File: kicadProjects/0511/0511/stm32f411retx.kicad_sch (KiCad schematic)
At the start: 22 parts, among them SW68 SW_Push, U6 STM32F411RETx, Y1 32.768KHz, Y2 8MHz

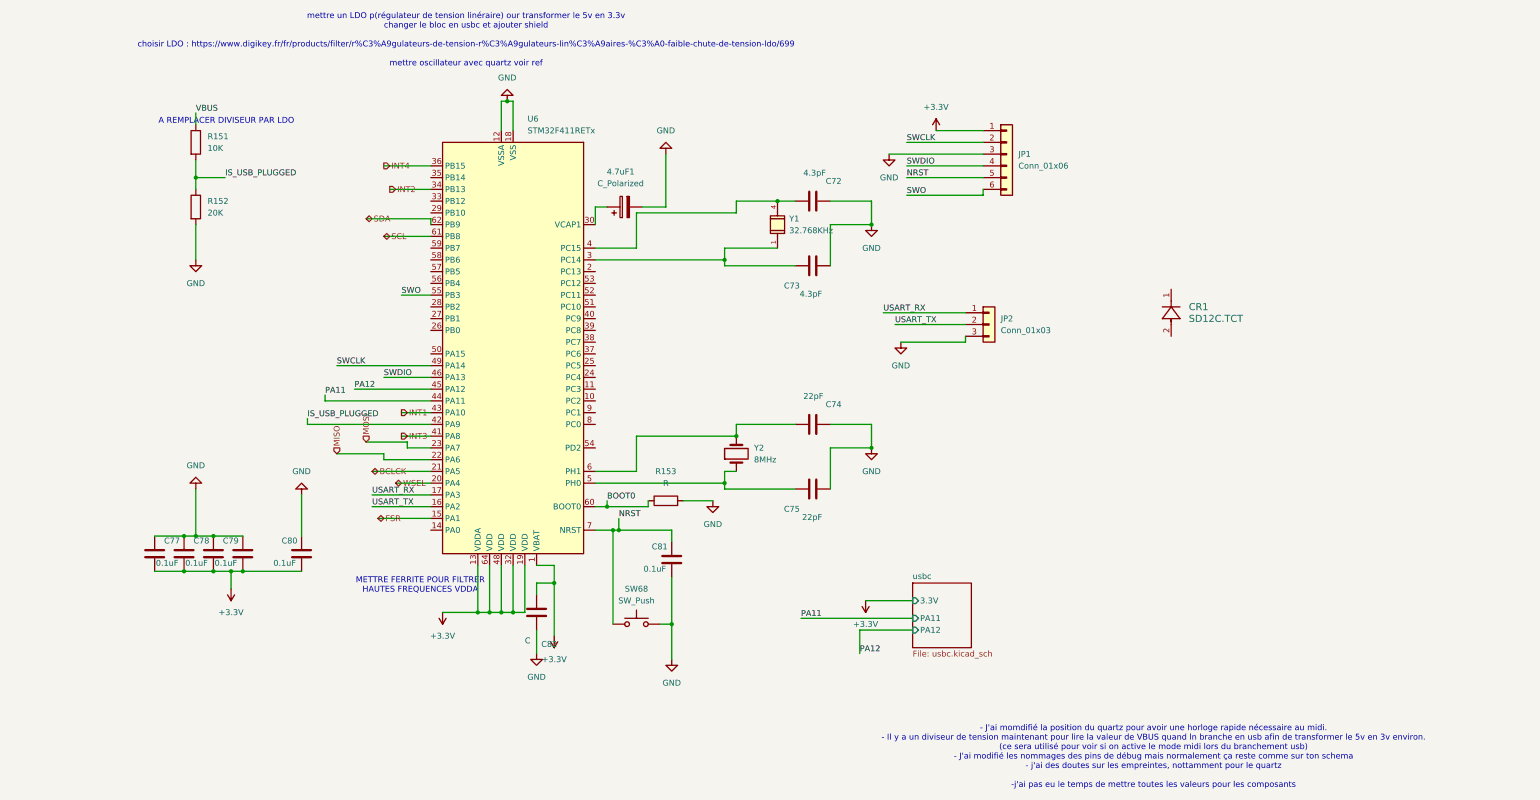
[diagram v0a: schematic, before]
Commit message: started to annotate and place buttons on pcb
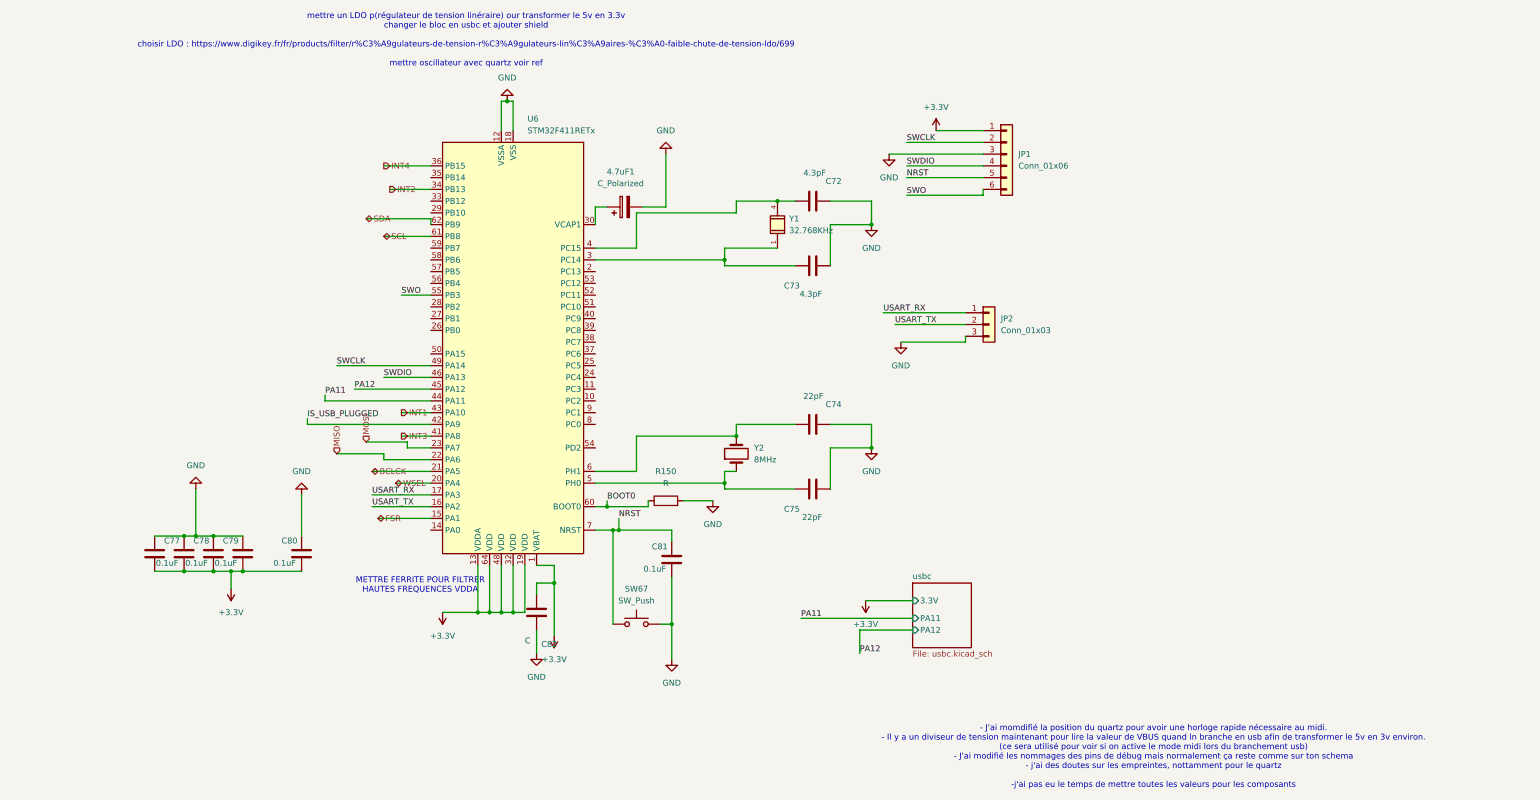
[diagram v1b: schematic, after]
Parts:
- removed CR1: SD12C.TCT, Project:CR_SD05_SEM, symbol ABS25-32.768KHZ-6-T:SD12C.TCT
- removed R151: 10K, Resistor_SMD:R_0603_1608Metric, symbol Device:R
- removed R152: 20K, Resistor_SMD:R_0603_1608Metric, symbol Device:R
- renumbered R153 to R150, SW68 to SW67
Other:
- note removed: "A REMPLACER DIVISEUR PAR LDO"

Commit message: poursuite placement et nommage références
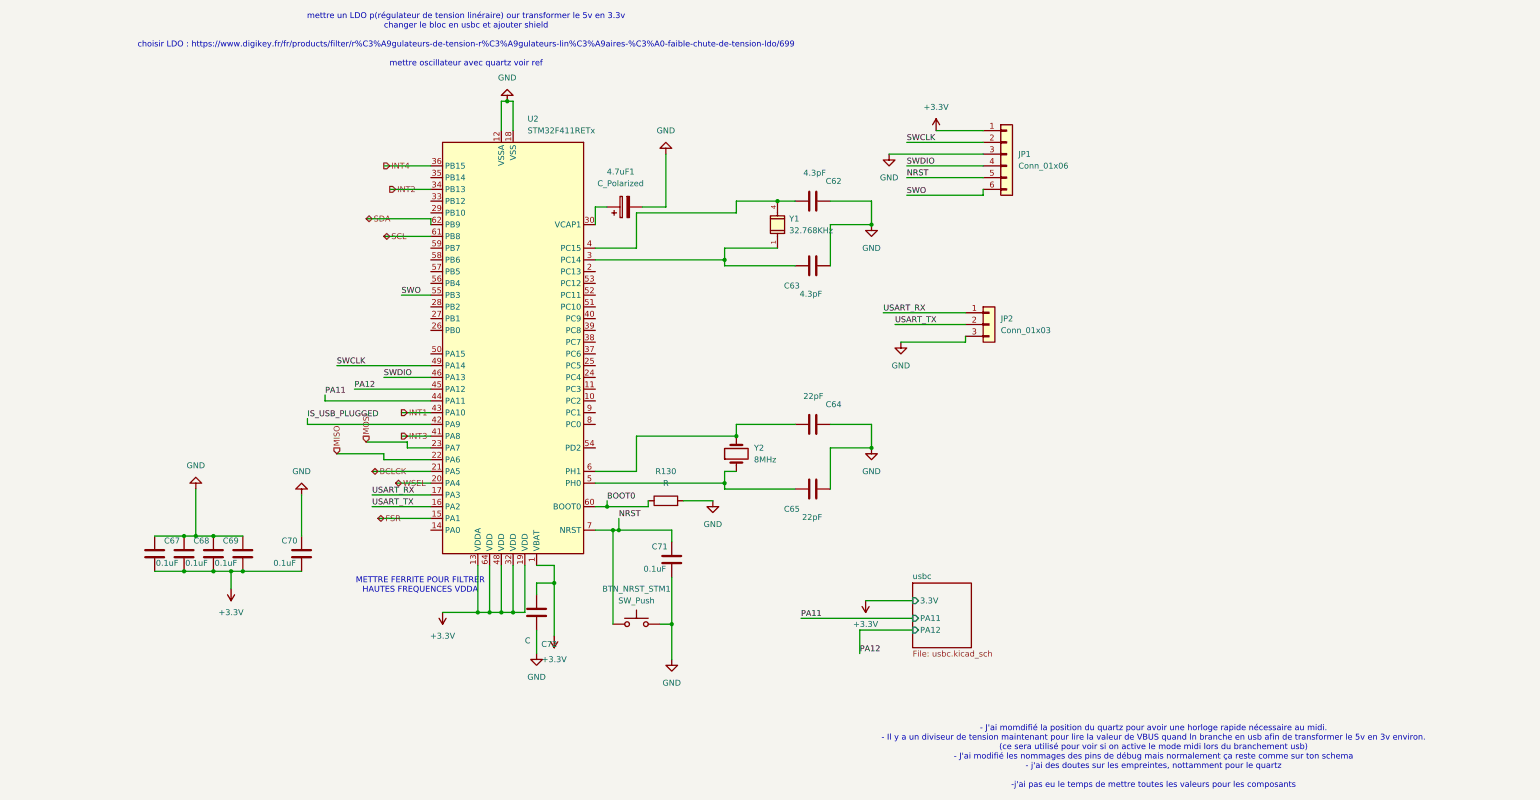
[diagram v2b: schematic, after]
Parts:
- renumbered SW67 to BTN_NRST_STM1, C72 to C62, C73 to C63, C74 to C64, C75 to C65, C76 to C66, C77 to C67, C78 to C68, C79 to C69, C80 to C70, C81 to C71, C82 to C72, R150 to R130, U6 to U2
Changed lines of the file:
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@@
 		(on_board yes)
 		(dnp no)
-		(property "Reference" "C77"
+		(property "Reference" "C67"
 			(at 23.622 129.286 0)
 			(effects
@@
 			(project "0511"
 				(path "/2c0b0e0d-c5e7-48b7-93bb-9be1941509af/7f025c79-ea20-4013-a71e-871359ae3c80"
-					(reference "C77")
+					(reference "C67")
 					(unit 1)
 				)
@@
 		(on_board yes)
 		(dnp no)
-		(property "Reference" "C74"
+		(property "Reference" "C64"
 			(at 166.624 99.822 90)
 			(effects
@@
 			(project "0511"
 				(path "/2c0b0e0d-c5e7-48b7-93bb-9be1941509af/7f025c79-ea20-4013-a71e-871359ae3c80"
-					(reference "C74")
+					(reference "C64")
 					(unit 1)
 				)
@@
 		(on_board yes)
 		(dnp no)
-		(property "Reference" "C80"
+		(property "Reference" "C70"
 			(at 49.022 129.286 0)
 			(effects
@@
 			(project "0511"
 				(path "/2c0b0e0d-c5e7-48b7-93bb-9be1941509af/7f025c79-ea20-4013-a71e-871359ae3c80"
-					(reference "C80")
+					(reference "C70")
 					(unit 1)
 				)
@@
 		(dnp no)
 		(fields_autoplaced yes)
-		(property "Reference" "#PWR0183"
+		(property "Reference" "#PWR0177"
 			(at 30.48 111.76 0)
 			(effects
@@
 			(project "0511"
 				(path "/2c0b0e0d-c5e7-48b7-93bb-9be1941509af/7f025c79-ea20-4013-a71e-871359ae3c80"
-					(reference "#PWR0183")
+					(reference "#PWR0177")
 					(unit 1)
 				)
@@
 		(dnp no)
 		(fields_autoplaced yes)
-		(property "Reference" "#PWR0184"
+		(property "Reference" "#PWR0178"
 			(at 53.34 113.03 0)
 			(effects
@@
 			(project "0511"
 				(path "/2c0b0e0d-c5e7-48b7-93bb-9be1941509af/7f025c79-ea20-4013-a71e-871359ae3c80"
-					(reference "#PWR0184")
+					(reference "#PWR0178")
 					(unit 1)
 				)
@@
 		(dnp no)
 		(fields_autoplaced yes)
-		(property "Reference" "U6"
+		(property "Reference" "U2"
 			(at 102.1781 38.1 0)
 			(effects
@@
 			(project "0511"
 				(path "/2c0b0e0d-c5e7-48b7-93bb-9be1941509af/7f025c79-ea20-4013-a71e-871359ae3c80"
-					(reference "U6")
+					(reference "U2")
 					(unit 1)
 				)
@@
 		(dnp no)
 		(fields_autoplaced yes)
-		(property "Reference" "R150"
+		(property "Reference" "R130"
 			(at 132.08 114.3 90)
 			(effects
@@
 			(project ""
 				(path "/2c0b0e0d-c5e7-48b7-93bb-9be1941509af/7f025c79-ea20-4013-a71e-871359ae3c80"
-					(reference "R150")
+					(reference "R130")
 					(unit 1)
 				)
@@
 		(dnp no)
 		(fields_autoplaced yes)
-		(property "Reference" "#PWR0178"
+		(property "Reference" "#PWR0172"
 			(at 132.08 39.37 0)
 			(effects
@@
 			(project "0511"
 				(path "/2c0b0e0d-c5e7-48b7-93bb-9be1941509af/7f025c79-ea20-4013-a71e-871359ae3c80"
-					(reference "#PWR0178")
+					(reference "#PWR0172")
 					(unit 1)
 				)
@@
 		(on_board yes)
 		(dnp no)
-		(property "Reference" "C73"
+		(property "Reference" "C63"
 			(at 161.036 74.168 90)
 			(effects
@@
 			(project "0511"
 				(path "/2c0b0e0d-c5e7-48b7-93bb-9be1941509af/7f025c79-ea20-4013-a71e-871359ae3c80"
-					(reference "C73")
+					(reference "C63")
 					(unit 1)
 				)
@@
 		(dnp no)
 		(fields_autoplaced yes)
-		(property "Reference" "#PWR0179"
+		(property "Reference" "#PWR0173"
 			(at 180.34 52.07 0)
 			(effects
@@
 			(project "0511"
 				(path "/2c0b0e0d-c5e7-48b7-93bb-9be1941509af/7f025c79-ea20-4013-a71e-871359ae3c80"
-					(reference "#PWR0179")
+					(reference "#PWR0173")
 					(unit 1)
 				)
@@
 		(dnp no)
 		(fields_autoplaced yes)
-		(property "Reference" "#PWR0185"
+		(property "Reference" "#PWR0179"
 			(at 142.24 127 0)
 			(effects
@@
 			(project "0511"
 				(path "/2c0b0e0d-c5e7-48b7-93bb-9be1941509af/7f025c79-ea20-4013-a71e-871359ae3c80"
-					(reference "#PWR0185")
+					(reference "#PWR0179")
 					(unit 1)
 				)
@@
 		(on_board yes)
 		(dnp no)
-		(property "Reference" "C72"
+		(property "Reference" "C62"
 			(at 166.624 51.562 90)
 			(effects
@@
 			(project "0511"
 				(path "/2c0b0e0d-c5e7-48b7-93bb-9be1941509af/7f025c79-ea20-4013-a71e-871359ae3c80"
-					(reference "C72")
+					(reference "C62")
 					(unit 1)
 				)
@@
 		(on_board yes)
 		(dnp no)
-		(property "Reference" "C78"
+		(property "Reference" "C68"
 			(at 29.972 129.286 0)
 			(effects
@@
 			(project "0511"
 				(path "/2c0b0e0d-c5e7-48b7-93bb-9be1941509af/7f025c79-ea20-4013-a71e-871359ae3c80"
-					(reference "C78")
+					(reference "C68")
 					(unit 1)
 				)
@@
 		(dnp no)
 		(fields_autoplaced yes)
-		(property "Reference" "#PWR0187"
+		(property "Reference" "#PWR0181"
 			(at 175.26 138.43 0)
 			(effects
@@
 			(project "0511"
 				(path "/2c0b0e0d-c5e7-48b7-93bb-9be1941509af/7f025c79-ea20-4013-a71e-871359ae3c80"
-					(reference "#PWR0187")
+					(reference "#PWR0181")
 					(unit 1)
 				)
@@
 		(dnp no)
 		(fields_autoplaced yes)
-		(property "Reference" "#PWR0181"
+		(property "Reference" "#PWR0175"
 			(at 182.88 92.71 0)
 			(effects
@@
 			(project "0511"
 				(path "/2c0b0e0d-c5e7-48b7-93bb-9be1941509af/7f025c79-ea20-4013-a71e-871359ae3c80"
-					(reference "#PWR0181")
+					(reference "#PWR0175")
 					(unit 1)
 				)
@@
 		(on_board yes)
 		(dnp no)
-		(property "Reference" "C76"
+		(property "Reference" "C66"
 			(at 17.272 129.286 0)
 			(effects
@@
 			(project "0511"
 				(path "/2c0b0e0d-c5e7-48b7-93bb-9be1941509af/7f025c79-ea20-4013-a71e-871359ae3c80"
-					(reference "C76")
+					(reference "C66")
 					(unit 1)
 				)
@@
 		(dnp no)
 		(fields_autoplaced yes)
-		(property "Reference" "#PWR0191"
+		(property "Reference" "#PWR0185"
 			(at 133.35 161.29 0)
 			(effects
@@
 			(project "0511"
 				(path "/2c0b0e0d-c5e7-48b7-93bb-9be1941509af/7f025c79-ea20-4013-a71e-871359ae3c80"
-					(reference "#PWR0191")
+					(reference "#PWR0185")
 					(unit 1)
 				)
@@
 		(dnp no)
 		(fields_autoplaced yes)
-		(property "Reference" "#PWR0190"
+		(property "Reference" "#PWR0184"
 			(at 104.14 160.02 0)
 			(effects
@@
 			(project "0511"
 				(path "/2c0b0e0d-c5e7-48b7-93bb-9be1941509af/7f025c79-ea20-4013-a71e-871359ae3c80"
-					(reference "#PWR0190")
+					(reference "#PWR0184")
 					(unit 1)
 				)
@@
 		(on_board yes)
 		(dnp no)
-		(property "Reference" "C81"
+		(property "Reference" "C71"
 			(at 129.032 130.556 0)
 			(effects
@@
 			(project "0511"
 				(path "/2c0b0e0d-c5e7-48b7-93bb-9be1941509af/7f025c79-ea20-4013-a71e-871359ae3c80"
-					(reference "C81")
+					(reference "C71")
 					(unit 1)
 				)
@@
 		(dnp no)
 		(fields_autoplaced yes)
-		(property "Reference" "#PWR0189"
+		(property "Reference" "#PWR0183"
 			(at 107.95 146.05 0)
 			(effects
@@
 			(project "0511"
 				(path "/2c0b0e0d-c5e7-48b7-93bb-9be1941509af/7f025c79-ea20-4013-a71e-871359ae3c80"
-					(reference "#PWR0189")
+					(reference "#PWR0183")
 					(unit 1)
 				)
@@
 		(dnp no)
 		(fields_autoplaced yes)
-		(property "Reference" "#PWR0180"
+		(property "Reference" "#PWR0174"
 			(at 176.53 67.31 0)
 			(effects
@@
 			(project "0511"
 				(path "/2c0b0e0d-c5e7-48b7-93bb-9be1941509af/7f025c79-ea20-4013-a71e-871359ae3c80"
-					(reference "#PWR0180")
+					(reference "#PWR0174")
 					(unit 1)
 				)
@@
 		(dnp no)
 		(fields_autoplaced yes)
-		(property "Reference" "#PWR0186"
+		(property "Reference" "#PWR0180"
 			(at 38.1 135.89 0)
 			(effects
@@
 			(project "0511"
 				(path "/2c0b0e0d-c5e7-48b7-93bb-9be1941509af/7f025c79-ea20-4013-a71e-871359ae3c80"
-					(reference "#PWR0186")
+					(reference "#PWR0180")
 					(unit 1)
 				)
@@
 		(on_board yes)
 		(dnp no)
-		(property "Reference" "C79"
+		(property "Reference" "C69"
 			(at 36.322 129.286 0)
 			(effects
@@
 			(project "0511"
 				(path "/2c0b0e0d-c5e7-48b7-93bb-9be1941509af/7f025c79-ea20-4013-a71e-871359ae3c80"
-					(reference "C79")
+					(reference "C69")
 					(unit 1)
 				)
@@
 		(dnp no)
 		(fields_autoplaced yes)
-		(property "Reference" "SW67"
+		(property "Reference" "BTN_NRST_STM1"
 			(at 125.73 139.7 0)
 			(effects
@@
 			(project ""
 				(path "/2c0b0e0d-c5e7-48b7-93bb-9be1941509af/7f025c79-ea20-4013-a71e-871359ae3c80"
-					(reference "SW67")
+					(reference "BTN_NRST_STM1")
 					(unit 1)
 				)
@@
 		(dnp no)
 		(fields_autoplaced yes)
-		(property "Reference" "#PWR0182"
+		(property "Reference" "#PWR0176"
 			(at 176.53 115.57 0)
 			(effects
@@
 			(project "0511"
 				(path "/2c0b0e0d-c5e7-48b7-93bb-9be1941509af/7f025c79-ea20-4013-a71e-871359ae3c80"
-					(reference "#PWR0182")
+					(reference "#PWR0176")
 					(unit 1)
 				)
@@
 		(dnp no)
 		(fields_autoplaced yes)
-		(property "Reference" "#PWR0176"
+		(property "Reference" "#PWR0170"
 			(at 97.79 27.94 0)
 			(effects
@@
 			(project "0511"
 				(path "/2c0b0e0d-c5e7-48b7-93bb-9be1941509af/7f025c79-ea20-4013-a71e-871359ae3c80"
-					(reference "#PWR0176")
+					(reference "#PWR0170")
 					(unit 1)
 				)
@@
 		(on_board yes)
 		(dnp no)
-		(property "Reference" "C75"
+		(property "Reference" "C65"
 			(at 161.036 122.428 90)
 			(effects
@@
 			(project "0511"
 				(path "/2c0b0e0d-c5e7-48b7-93bb-9be1941509af/7f025c79-ea20-4013-a71e-871359ae3c80"
-					(reference "C75")
+					(reference "C65")
 					(unit 1)
 				)
@@
 		(dnp no)
 		(fields_autoplaced yes)
-		(property "Reference" "#PWR0188"
+		(property "Reference" "#PWR0182"
 			(at 83.82 140.97 0)
 			(effects
@@
 			(project "0511"
 				(path "/2c0b0e0d-c5e7-48b7-93bb-9be1941509af/7f025c79-ea20-4013-a71e-871359ae3c80"
-					(reference "#PWR0188")
+					(reference "#PWR0182")
 					(unit 1)
 				)
@@
 		(on_board yes)
 		(dnp no)
-		(property "Reference" "C82"
+		(property "Reference" "C72"
 			(at 105.156 151.638 0)
 			(effects
@@
 			(project ""
 				(path "/2c0b0e0d-c5e7-48b7-93bb-9be1941509af/7f025c79-ea20-4013-a71e-871359ae3c80"
-					(reference "C82")
+					(reference "C72")
 					(unit 1)
 				)
@@
 		(dnp no)
 		(fields_autoplaced yes)
-		(property "Reference" "#PWR0177"
+		(property "Reference" "#PWR0171"
 			(at 190.5 44.45 0)
 			(effects
@@
 			(project "0511"
 				(path "/2c0b0e0d-c5e7-48b7-93bb-9be1941509af/7f025c79-ea20-4013-a71e-871359ae3c80"
-					(reference "#PWR0177")
-					(unit 1)
-				)
+					(reference "#PWR0171")
+					(unit 1)
+				)
